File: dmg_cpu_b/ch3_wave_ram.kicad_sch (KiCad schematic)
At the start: 93 parts

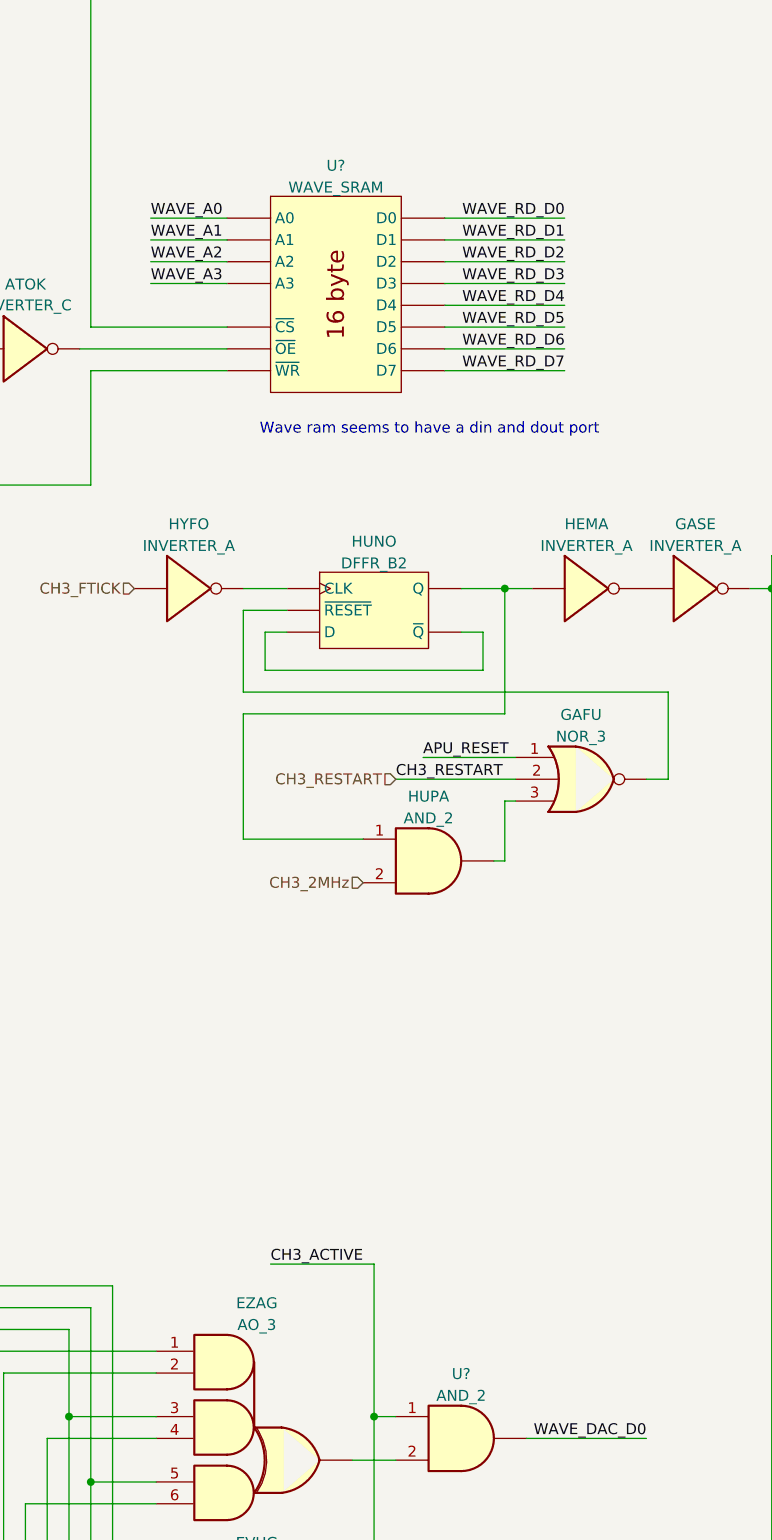
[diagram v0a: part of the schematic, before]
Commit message: fixes made following review
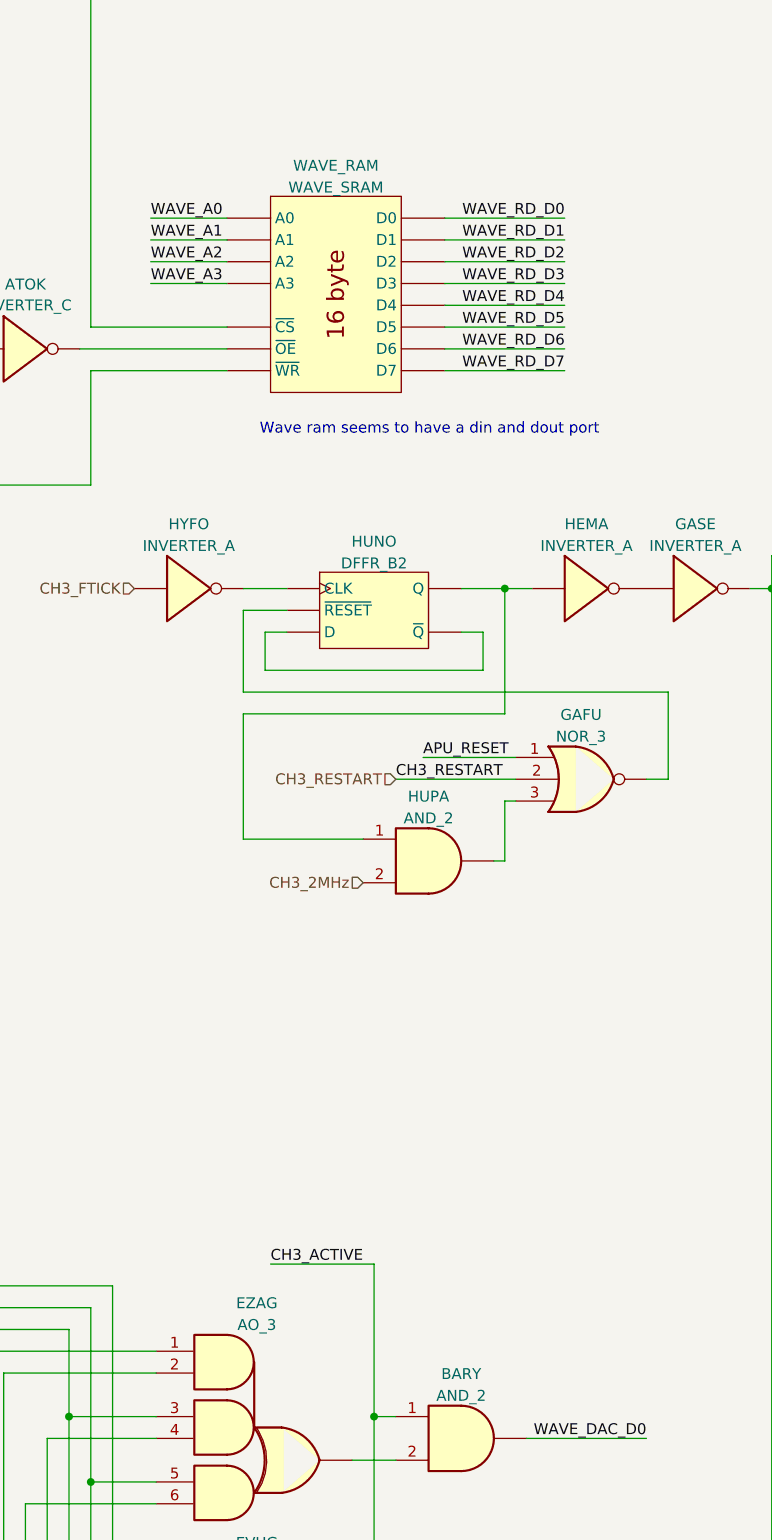
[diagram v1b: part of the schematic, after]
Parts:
- gave numbers to parts that had none: 2
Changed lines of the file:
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@@
   (symbol (lib_id "DMG_CPU_Cells:AND_2") (at 233.68 208.28 0) (unit 1)
     (in_bom yes) (on_board yes) (fields_autoplaced)
-    (property "Reference" "U?" (id 0) (at 233.68 200.7702 0))
+    (property "Reference" "BARY" (id 0) (at 233.68 200.7702 0))
     (property "Value" "AND_2" (id 1) (at 233.68 203.3071 0))
     (property "Footprint" "" (id 2) (at 233.68 208.28 0)
@@
   (symbol (lib_id "DMG_CPU_Cells:WAVE_SRAM") (at 219.075 74.93 0) (unit 1)
     (in_bom yes) (on_board yes) (fields_autoplaced)
-    (property "Reference" "U?" (id 0) (at 219.075 59.9272 0))
+    (property "Reference" "WAVE_RAM" (id 0) (at 219.075 59.9272 0))
     (property "Value" "WAVE_SRAM" (id 1) (at 219.075 62.4641 0))
     (property "Footprint" "" (id 2) (at 219.075 77.47 0)

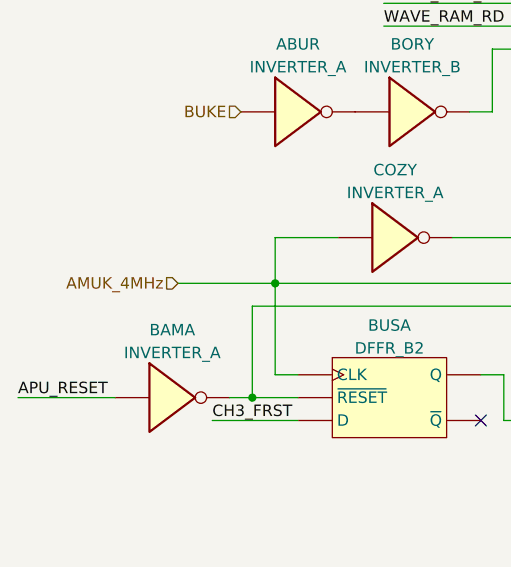
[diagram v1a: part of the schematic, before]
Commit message: Fixes made from issues, channel 4 sheet aded and tidy up of hierarchical APU sheet. Small fixes done here and there when doing ERC.
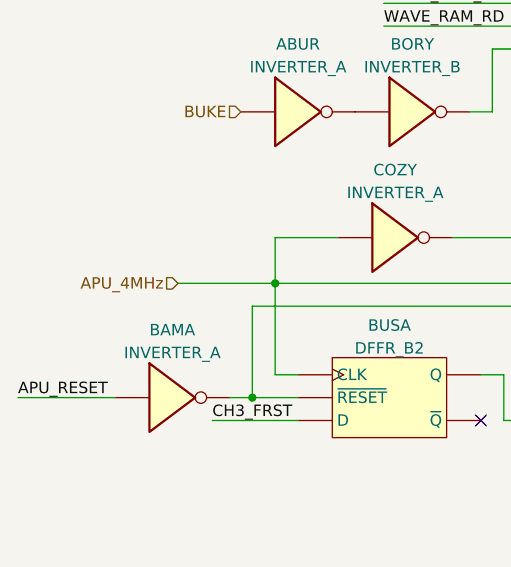
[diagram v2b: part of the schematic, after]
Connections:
- net AMUK_4MHz renamed APU_4MHz
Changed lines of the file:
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@@
     (effects (font (size 1.27 1.27)) (justify right))
   )
-  (hierarchical_label "AMUK_4MHz" (shape input) (at 34.29 52.705 180)
+  (hierarchical_label "APU_4MHz" (shape input) (at 34.29 52.705 180)
     (effects (font (size 1.27 1.27)) (justify right))
   )

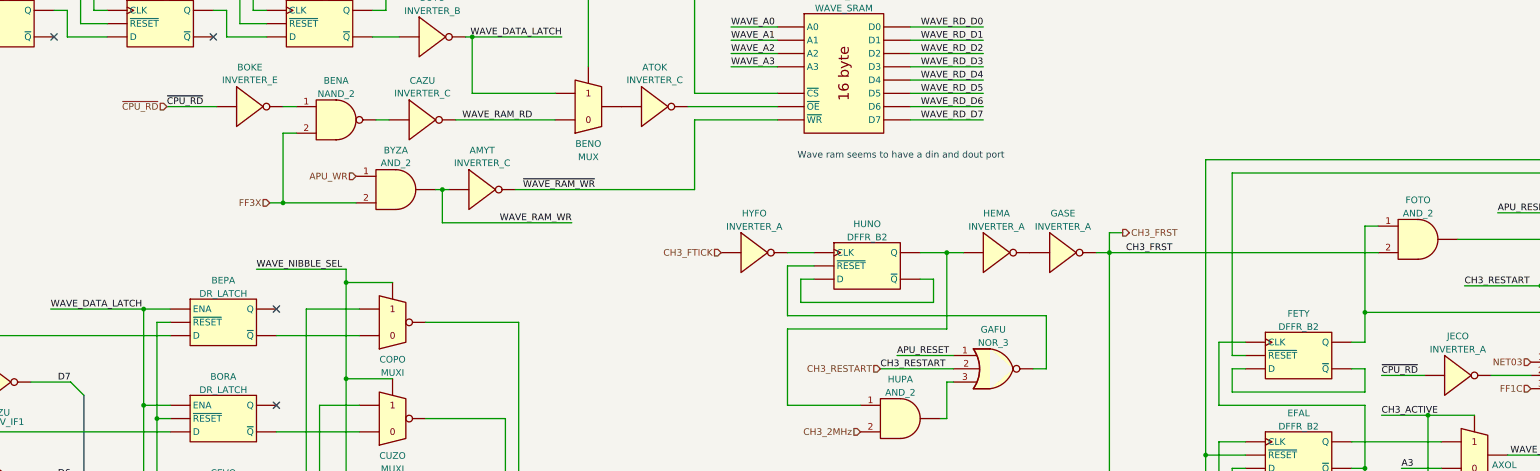
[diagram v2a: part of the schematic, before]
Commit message: Fixes made based on raised issues. PPU decode page added as draft level.
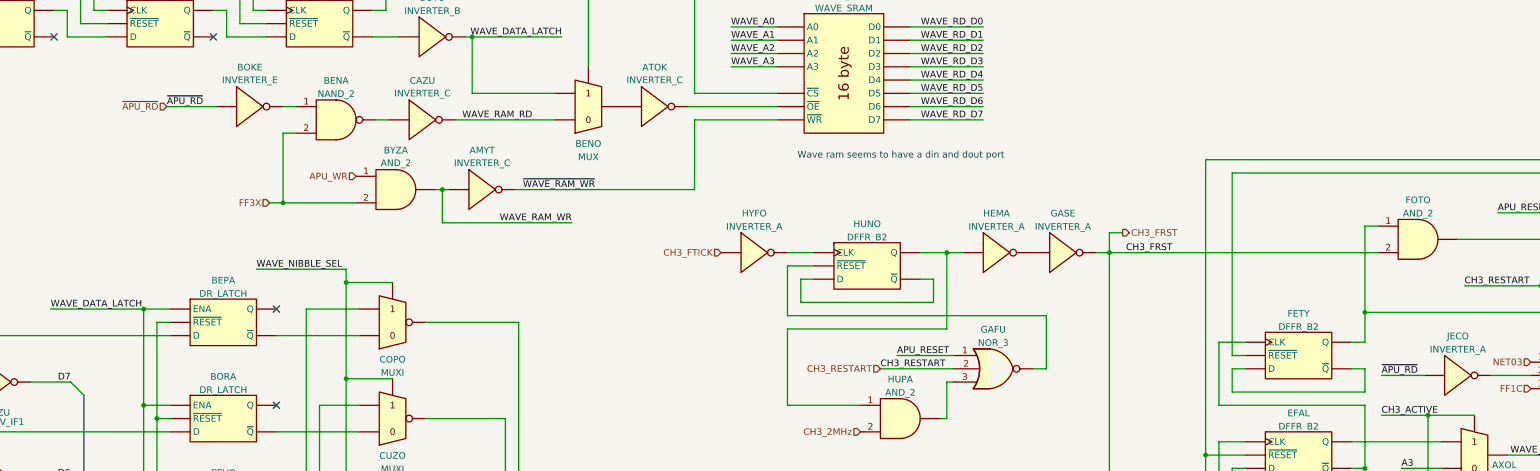
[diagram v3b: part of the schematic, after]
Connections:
- net ~{CPU_RD} renamed ~{APU_RD}
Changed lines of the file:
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@@
     (effects (font (size 1.27 1.27)) (justify right bottom))
   )
-  (label "~{CPU_RD}" (at 321.945 132.715 0)
+  (label "~{APU_RD}" (at 321.945 132.715 0)
     (effects (font (size 1.27 1.27)) (justify left bottom))
   )
-  (label "~{CPU_RD}" (at 89.535 81.28 0)
+  (label "~{APU_RD}" (at 89.535 81.28 0)
     (effects (font (size 1.27 1.27)) (justify left bottom))
   )
@@
     (effects (font (size 1.27 1.27)) (justify right))
   )
-  (hierarchical_label "~{CPU_RD}" (shape input) (at 89.535 81.28 180)
+  (hierarchical_label "~{APU_RD}" (shape input) (at 89.535 81.28 180)
     (effects (font (size 1.27 1.27)) (justify right))
   )

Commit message: Fixes made based on raised issues (in APU sheets).
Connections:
- net D3: no longer FERA.3
- net D4: now also FERA.3
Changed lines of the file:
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@@
     (effects (font (size 1.27 1.27)) (justify right bottom))
   )
-  (label "D3" (at 399.415 154.94 180)
+  (label "D4" (at 399.415 154.94 180)
     (effects (font (size 1.27 1.27)) (justify right bottom))
   )

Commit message: VRAM interface sheet added but various edits in existing sheets. Notable merge of RESET, CLOCKS and FF04 DIV sheets
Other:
- company: (none) -> CC-BY-SA-4.0 Régis Galland & Michael Singer -- Derived work from Furrtek
- title: (none) -> DMG CPU B
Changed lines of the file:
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@@
 (kicad_sch (version 20211123) (generator eeschema)
   (paper "A3")
+  (title_block
+    (title "DMG CPU B")
+    (date "2022-05-02")
+    (rev "0")
+    (company "CC-BY-SA-4.0 Régis Galland & Michael Singer -- Derived work from Furrtek")
+    (comment 1 "https://github.com/msinger/dmg-schematics")
+  )
   (junction (at 190.5 213.36) (diameter 0) (color 0 0 0 0)
   )

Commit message: Fixes from raised github issues + tidy up of hierarchical sheets. WIP on WAVE RAM sheets.
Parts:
- added GENO? (x8): INVERTER_A, symbol DMG_CPU_Cells:INVERTER_A
- added U? (x8): AND_2, symbol DMG_CPU_Cells:AND_2
- added U? (x2): OR_2, symbol DMG_CPU_Cells:OR_2
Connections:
- net CH3_ACTIVE: now also GENO?.1, U?.2
- net WAVE_A0: now also GENO?.1, U?.2, U?.2
- net WAVE_A1: now also GENO?.1, U?.1, U?.1
- net WAVE_A2: now also GENO?.1
- net WAVE_A3: now also GENO?.1
- net ~{WAVE_RAM_WR}: now also GENO?.1
- net ~{WAVE_RAM_OE}: now reaches ATOK.2, WAVE_RAM.6 (~{OE})
- net ~{WAVE_RAM_OE}: now also GENO?.1
- net ~{WAVE_RAM_CS}: now reaches ALER.2, WAVE_RAM.5 (~{CS})
- net ~{WAVE_RAM_CS}: now also GENO?.1
- new net: GENO?.2, U?.2 (x3)
- new net: GENO?.2, U?.1, U?.1 (x2)
- new net: GENO?.2, U?.2, U?.2
- new net: U?.1, U?.3 (x3)
- new net: U?.1, U?.2, U?.3
- new net: U?.2, U?.3
- new net COL0: U?.3
- new net COL1: U?.3
- new net COL2: U?.3
- new net COL3: U?.3
- new net TO_WRAM_RAM: U?.3
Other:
- note added: "2-4 Decoder"
- note added: "Test Sample Read"
- note added: "WIP - WRAM RAM connections"
- note added: "{signal: [ {name: 'APU_4MHZ', wave: '1010101010101010101|01010101010101010101|0101010101010101'}, {name: 'CH3_2MHZ', wave: '0.1.0.1.0.1.0.1.0.1|.0.1.0.1.0.1.0.1.0.1|.0.1.0.1.0.1.0.1'}, {name: 'CH3_ACTIVE', wave: '1..................|....................|................'}, {name: 'CH3_RESTART',wave: '0...1...0..........|....................|................'}, {name: 'CH3_FCOUNT', wave: 'x...3...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"
- moved on the sheet: ABUR, ACOR, ADOK, AFUM, AGYL, AKAF, ALER, AMYT, ARUC, ATEC, ATOK, ATUR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

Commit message: Fixes based on review. + various other edits.
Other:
- note added: "RAM EN? Signal '1' when 1) ACTIVE is low and RD or WR are taking place (CPU access). 2) ACTIVE is high and RD is taking place (Sample RD cycles) This means that writing during Sample RD can corrupt the RAM as RAM address is defined by Sample RD address and not the CPU address."
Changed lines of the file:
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@@
+    (effects (font (size 1.27 1.27)) (justify left bottom))
+  )
+  (text "RAM EN?\nSignal '1' when \n1) ACTIVE is low and RD or WR are taking place (CPU access).\n2) ACTIVE is high and RD is taking place (Sample RD cycles)\n\nThis means that writing during Sample RD can corrupt the RAM as RAM address is defined by Sample RD address and not the CPU address. "
+    (at 472.44 168.275 0)
     (effects (font (size 1.27 1.27)) (justify left bottom))
   )
